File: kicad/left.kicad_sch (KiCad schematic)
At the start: 101 parts, among them Q1 PMF170XP,115, Q2 FS8205A_C2830320, SW1 TS-1088-AR02016, U1 SN74LVC1G17DBVR, U2 E73-2G4M08S1C, U3 SN74LVC1G74DQER, U4 S2B-PH-K-S(LF)(SN), U5 BL8573CS8TR, U6 DW01A_C42380662, U7 LP5024RSMR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

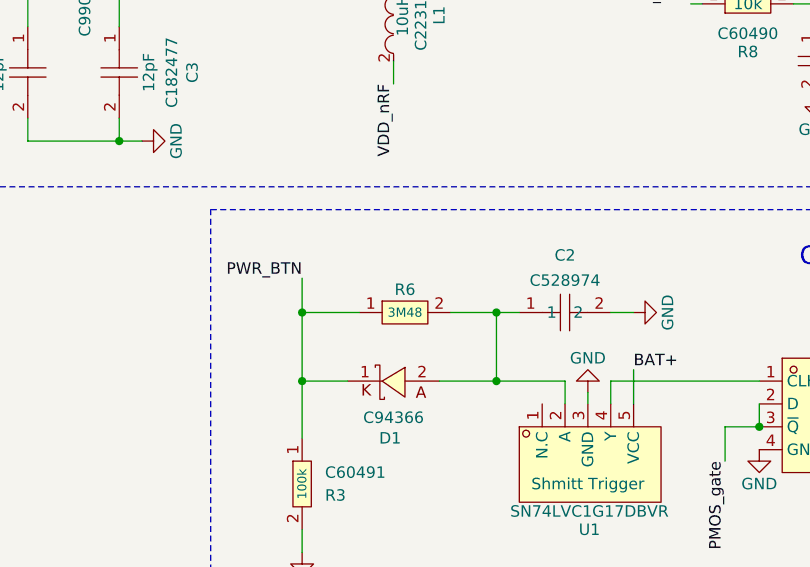
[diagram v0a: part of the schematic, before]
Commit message: changed on/off timing resistor to 2M61 0805
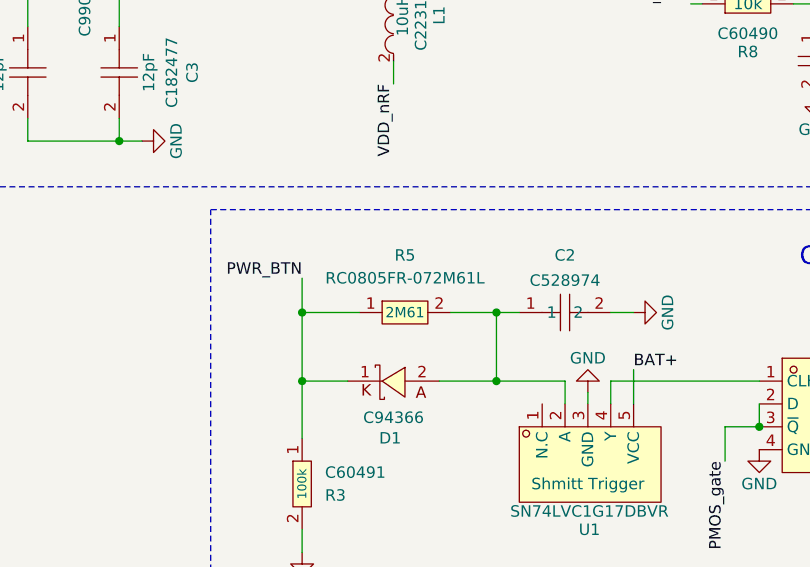
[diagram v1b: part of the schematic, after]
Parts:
- removed R6: 0402WGF1604TCE, easyeda2kicad:R0402, symbol easyeda2kicad:0402WGF1604TCE
- added R5: RC0805FR-072M61L, easyeda2kicad:R0805, symbol easyeda2kicad:RC0805FR-072M61L
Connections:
- net PWR_BTN: now also R5.1
- net at C2.1, D1.2, U1.2 (A): now also R5.2
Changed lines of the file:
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@@
-	)
-	(symbol
-		(lib_id "easyeda2kicad:0402WGF1604TCE")
-		(at 327.66 120.65 0)
-		(unit 1)
-		(body_style 1)
-		(exclude_from_sim no)
-		(in_bom yes)
-		(on_board yes)
-		(in_pos_files yes)
-		(dnp no)
-		(fields_autoplaced yes)
-		(property "Reference" "R6"
-			(at 327.66 118.11 0)
-			(show_name no)
-			(do_not_autoplace no)
-			(effects
-				(font
-					(size 1.27 1.27)
-				)
-			)
-		)
-		(property "Value" "0402WGF1604TCE"
-			(at 327.66 116.84 0)
-			(hide yes)
-			(show_name no)
-			(do_not_autoplace no)
-			(effects
-				(font
-					(size 1.27 1.27)
-				)
-			)
-		)
-		(property "Footprint" "easyeda2kicad:R0402"
-			(at 327.66 128.27 0)
-			(hide yes)
-			(show_name no)
-			(do_not_autoplace no)
-			(effects
-				(font
-					(size 1.27 1.27)
-				)
-			)
-		)
-		(property "Datasheet" "https://lcsc.com/product-detail/Chip-Resistor-Surface-Mount_Uniroyal-Elec-0402WGF1604TCE_C423231.html"
-			(at 327.66 130.81 0)
-			(hide yes)
-			(show_name no)
-			(do_not_autoplace no)
-			(effects
-				(font
-					(size 1.27 1.27)
-				)
-			)
-		)
-		(property "Description" "3M48"
-			(at 327.66 120.65 0)
-			(show_name no)
-			(do_not_autoplace no)
-			(effects
-				(font
-					(size 1.016 1.016)
-				)
-			)
-		)
-		(property "LCSC Part" "C423231"
-			(at 327.66 133.35 0)
-			(hide yes)
-			(show_name no)
-			(do_not_autoplace no)
-			(effects
-				(font
-					(size 1.27 1.27)
-				)
-			)
-		)
-		(pin "2"
-		)
-		(pin "1"
-		)
-		(instances
-			(project "left"
-				(path "/3171f1b4-f2dd-4471-8b63-415e18370dba"
-					(reference "R6")
-					(unit 1)
-				)
-			)
-		)
 	)
 	(symbol
@@
 					(unit 1)
 				)
+			)
+		)
+	)
+	(symbol
+		(lib_id "easyeda2kicad:RC0805FR-072M61L")
+		(at 327.66 120.65 0)
+		(unit 1)
+		(body_style 1)
+		(exclude_from_sim no)
+		(in_bom yes)
+		(on_board yes)
+		(in_pos_files yes)
+		(dnp no)
+		(fields_autoplaced yes)
+		(property "Reference" "R5"
+			(at 327.66 114.3 0)
+			(show_name no)
+			(do_not_autoplace no)
+			(effects
+				(font
+					(size 1.27 1.27)
+				)
+			)
+		)
+		(property "Value" "RC0805FR-072M61L"
+			(at 327.66 116.84 0)
+			(show_name no)
+			(do_not_autoplace no)
+			(effects
+				(font
+					(size 1.27 1.27)
+				)
+			)
+		)
+		(property "Footprint" "easyeda2kicad:R0805"
+			(at 327.66 128.27 0)
+			(hide yes)
+			(show_name no)
+			(do_not_autoplace no)
+			(effects
+				(font
+					(size 1.27 1.27)
+				)
+			)
+		)
+		(property "Datasheet" "https://lcsc.com/product-detail/New-Arrivals_YAGEO-RC0805FR-072M61L_C483050.html"
+			(at 327.66 130.81 0)
+			(hide yes)
+			(show_name no)
+			(do_not_autoplace no)
+			(effects
+				(font
+					(size 1.27 1.27)
+				)
+			)
+		)
+		(property "Description" "2M61"
+			(at 327.66 120.65 0)
+			(show_name no)
+			(do_not_autoplace no)
+			(effects
+				(font
+					(size 1.143 1.143)
+				)
+			)
+		)
+		(property "Manufacturer" "YAGEO(国巨)"
+			(at 327.66 133.35 0)
+			(hide yes)
+			(show_name no)
+			(do_not_autoplace no)
+			(effects
+				(font
+					(size 1.27 1.27)
+				)
+			)
+		)
+		(property "MPN" "RC0805FR-072M61L"
+			(at 327.66 135.89 0)
+			(hide yes)
+			(show_name no)
+			(do_not_autoplace no)
+			(effects
+				(font
+					(size 1.27 1.27)
+				)
+			)
+		)
+		(property "LCSC Part" "C483050"
+			(at 327.66 138.43 0)
+			(hide yes)
+			(show_name no)
+			(do_not_autoplace no)
+			(effects
+				(font
+					(size 1.27 1.27)
+				)
+			)
+		)
+		(pin "1"
+		)
+		(pin "2"
+		)
+		(instances
+			(project "left"
+				(path "/3171f1b4-f2dd-4471-8b63-415e18370dba"
+					(reference "R5")
+					(unit 1)
+				)

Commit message: added gnd vias all over the board. went trough schematic again. changed resistor for rc to bigger one in footprint, and smaller one in Ohm. both left and right sides are ready. just need to go over the kicads check and lastly let someone on discord have a look on the project
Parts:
- removed R15: RT0402BRD0737K4L, :R0402, symbol easyeda2kicad:RT0402BRD0737K4L
- added R6: ERA2AED753X, easyeda2kicad:R0402, symbol easyeda2kicad:ERA2AED753X
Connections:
- net BAT+: now also U6.5 (VDD); no longer U6.6 (VSS)
- net GND: now also U6.6 (VSS), R6.2; no longer U6.5 (VDD)
- net at U7.31 (IREF): now also R6.1
- no-connect marks 0 -> 20
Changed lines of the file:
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@@
 		(color 0 0 0 0)
 	)
+	(no_connect
+		(at 372.11 187.96)
+	)
+	(no_connect
+		(at 340.36 24.13)
+	)
+	(no_connect
+		(at 340.36 26.67)
+	)
+	(no_connect
+		(at 387.35 135.89)
+	)
+	(no_connect
+		(at 349.25 187.96)
+	)
+	(no_connect
+		(at 271.78 184.15)
+	)
+	(no_connect
+		(at 298.45 71.12)
+	)
+	(no_connect
+		(at 260.35 236.22)
+	)
+	(no_connect
+		(at 340.36 36.83)
+	)
+	(no_connect
+		(at 340.36 41.91)
+	)
+	(no_connect
+		(at 134.62 44.45)
+	)
+	(no_connect
+		(at 318.77 71.12)
+	)
+	(no_connect
+		(at 271.78 199.39)
+	)
+	(no_connect
+		(at 134.62 46.99)
+	)
+	(no_connect
+		(at 340.36 31.75)
+	)
+	(no_connect
+		(at 308.61 71.12)
+	)
+	(no_connect
+		(at 340.36 54.61)
+	)
+	(no_connect
+		(at 134.62 49.53)
+	)
+	(no_connect
+		(at 313.69 71.12)
+	)
+	(no_connect
+		(at 340.36 46.99)
+	)
 	(bus_entry
 		(at 118.11 73.66)
@@
 	(wire
 		(pts
-			(xy 260.35 243.84) (xy 260.35 241.3)
-		)
-		(stroke
-			(width 0)
-			(type default)
-		)
-	)
-	(wire
-		(pts
 			(xy 316.23 120.65) (xy 316.23 128.27)
 		)
@@
 	)
 	(label "BAT+"
-		(at 260.35 243.84 180)
+		(at 260.35 238.76 180)
 		(effects
 			(font
@@
 	(symbol
 		(lib_id "PCM_SparkFun-PowerSymbol:GND")
-		(at 260.35 238.76 270)
+		(at 260.35 241.3 270)
 		(unit 1)
 		(body_style 1)
@@
 		(fields_autoplaced yes)
 		(property "Reference" "#PWR022"
-			(at 254 238.76 0)
+			(at 254 241.3 0)
 			(hide yes)
 			(show_name no)
@@
 		)
 		(property "Value" "GND"
-			(at 256.54 238.76 0)
+			(at 256.54 241.3 0)
 			(show_name no)
 			(do_not_autoplace yes)
@@
 		)
 		(property "Footprint" ""
-			(at 260.35 238.76 0)
+			(at 260.35 241.3 0)
 			(hide yes)
 			(show_name no)
@@
 		)
 		(property "Datasheet" ""
-			(at 260.35 238.76 0)
+			(at 260.35 241.3 0)
 			(hide yes)
 			(show_name no)
@@
 		)
 		(property "Description" "Power symbol creates a global label with name \"GND\" , ground"
-			(at 251.46 238.76 0)
+			(at 251.46 241.3 0)
 			(hide yes)
 			(show_name no)
@@
 	)
 	(symbol
+		(lib_id "easyeda2kicad:ERA2AED753X")
+		(at 195.58 31.75 0)
+		(unit 1)
+		(body_style 1)
+		(exclude_from_sim no)
+		(in_bom yes)
+		(on_board yes)
+		(in_pos_files yes)
+		(dnp no)
+		(fields_autoplaced yes)
+		(property "Reference" "R6"
+			(at 195.58 25.4 0)
+			(show_name no)
+			(do_not_autoplace no)
+			(effects
+				(font
+					(size 1.27 1.27)
+				)
+			)
+		)
+		(property "Value" "ERA2AED753X"
+			(at 195.58 27.94 0)
+			(show_name no)
+			(do_not_autoplace no)
+			(effects
+				(font
+					(size 1.27 1.27)
+				)
+			)
+		)
+		(property "Footprint" "easyeda2kicad:R0402"
+			(at 195.58 39.37 0)
+			(hide yes)
+			(show_name no)
+			(do_not_autoplace no)
+			(effects
+				(font
+					(size 1.27 1.27)
+				)
+			)
+		)
+		(property "Datasheet" "https://lcsc.com/product-detail/New-Arrivals_PANASONIC-ERA2AED753X_C491105.html"
+			(at 195.58 41.91 0)
+			(hide yes)
+			(show_name no)
+			(do_not_autoplace no)
+			(effects
+				(font
+					(size 1.27 1.27)
+				)
+			)
+		)
+		(property "Description" "75k"
+			(at 195.58 31.75 0)
+			(show_name no)
+			(do_not_autoplace no)
+			(effects
+				(font
+					(size 1.27 1.27)
+				)
+			)
+		)
+		(property "Manufacturer" "PANASONIC(松下)"
+			(at 195.58 44.45 0)
+			(hide yes)
+			(show_name no)
+			(do_not_autoplace no)
+			(effects
+				(font
+					(size 1.27 1.27)
+				)
+			)
+		)
+		(property "MPN" "ERA2AED753X"
+			(at 195.58 46.99 0)
+			(hide yes)
+			(show_name no)
+			(do_not_autoplace no)
+			(effects
+				(font
+					(size 1.27 1.27)
+				)
+			)
+		)
+		(property "LCSC Part" "C491105"
+			(at 195.58 49.53 0)
+			(hide yes)
+			(show_name no)
+			(do_not_autoplace no)
+			(effects
+				(font
+					(size 1.27 1.27)
+				)
+			)
+		)
+		(pin "1"
+		)
+		(pin "2"
+		)
+		(instances
+			(project "left"
+				(path "/3171f1b4-f2dd-4471-8b63-415e18370dba"
+					(reference "R6")
+					(unit 1)
+				)
+			)
+		)
+	)
+	(symbol
 		(lib_id "PCM_SparkFun-PowerSymbol:GND")
 		(at 353.06 120.65 90)
@@
 					(unit 1)
 				)
-			)
-		)
-	)
-	(symbol
-		(lib_id "easyeda2kicad:RT0402BRD0737K4L")
-		(at 195.58 31.75 0)
-		(unit 1)
-		(body_style 1)
-		(exclude_from_sim no)
-		(in_bom yes)
-		(on_board yes)
-		(in_pos_files yes)
-		(dnp no)
-		(fields_autoplaced yes)
-		(property "Reference" "R15"
-			(at 195.58 26.162 0)
-			(show_name no)
-			(do_not_autoplace no)
-			(effects
-				(font
-					(size 1.27 1.27)
-				)
-			)
-		)
-		(property "Value" "RT0402BRD0737K4L"
-			(at 195.58 27.94 0)
-			(hide yes)
-			(show_name no)
-			(do_not_autoplace no)
-			(effects
-				(font
-					(size 1.27 1.27)
-				)
-			)
-		)
-		(property "Footprint" ":R0402"
-			(at 195.58 39.37 0)
-			(hide yes)
-			(show_name no)
-			(do_not_autoplace no)
-			(effects
-				(font
-					(size 1.27 1.27)
-				)
-			)
-		)
-		(property "Datasheet" ""
-			(at 195.58 31.75 0)
-			(hide yes)
-			(show_name no)
-			(do_not_autoplace no)
-			(effects
-				(font
-					(size 1.27 1.27)
-				)
-			)
-		)
-		(property "Description" "37k4"
-			(at 195.58 31.75 0)
-			(show_name no)
-			(do_not_autoplace no)
-			(effects
-				(font
-					(size 1.27 1.27)
-				)
-			)
-		)
-		(property "LCSC Part" "C852746"
-			(at 195.58 28.702 0)
-			(show_name no)
-			(do_not_autoplace no)
-			(effects
-				(font
-					(size 1.27 1.27)
-				)
-			)
-		)
-		(pin "1"
-		)
-		(pin "2"
-		)
-		(instances
-			(project "left"
-				(path "/3171f1b4-f2dd-4471-8b63-415e18370dba"
-					(reference "R15")
-					(unit 1)
-				)

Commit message: both sides done. changed few components for their basic or more affordable alternaatives.
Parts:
- added U9: USBLC6-2SC6, Package_TO_SOT_SMD:SOT-23-6, symbol Power_Protection:USBLC6-2SC6
- C1, C3: value 0402CG120F500NT -> 0402CG120J500NT; LCSC Part C182477 -> C1547
- C2: value GRM155Z71A105KE01D -> CL05A105KA5NQNC; LCSC Part C528974 -> C52923
- C4, C6, C9: value GRM033C71C104KE14D -> CL05B104KB54PNC; footprint easyeda2kicad:C0201 -> easyeda2kicad:C0402; LCSC Part C85923 -> C307331
- C7, C8: value GRM155C71C105KE11D -> CL05A105KA5NQNC; LCSC Part C576449 -> C52923
- R1, R17: value RC0402FR-071ML -> 0402WGF1004TCE; LCSC Part C138033 -> C26083
- R10, R14, R16, R9: value RC0402FR-075K1L -> 0402WGF5101TCE; LCSC Part C105872 -> C25905
- R11: value RC0201FR-07680RL -> RC0402FR-07680RL; footprint easyeda2kicad:R0201 -> easyeda2kicad:R0402; LCSC Part C274876 -> C137948
- R12, R13, R4, R7, R8: value RC0402FR-0710KL -> 0402WGF1002TCE; LCSC Part C60490 -> C25744
- R5: value RC0805FR-072M61L -> RTT022614FTH; footprint easyeda2kicad:R0805 -> easyeda2kicad:R0402; LCSC Part C483050 -> C166493; MPN RC0805FR-072M61L -> RTT022614FTH; Manufacturer YAGEO(国巨) -> RALEC
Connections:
- net SCL_BAT is gone; now on net SCL: U2.8 (AI5), U8.7 (SCL)
- net SDA_BAT is gone; now on net SDA: U2.7 (AI0), U8.8 (SDA)
- net D+: now also U9.1 (I/O1), U9.6 (I/O1)
- net D-: now also U9.3 (I/O2), U9.4 (I/O2)
- net GND: now also U9.2 (GND)
- net SCL: no longer U2.17 (P1.09)
- net SDA: no longer U2.16 (P0.08)
- net SWBCLK: now also U2.39 (SWC); no longer U2.2 (P1.10)
- net SWDIO: now also U2.37 (SWD); no longer U2.1 (P1.11)
- net VBUS_RAW: now reaches F1.1, USBC1.A4B9 (VBUS), USBC1.B4A9 (VBUS)
- net VBUS_RAW: now also U9.5 (VBUS)
- no-connect marks 20 -> 18
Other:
- moved on the sheet: C6

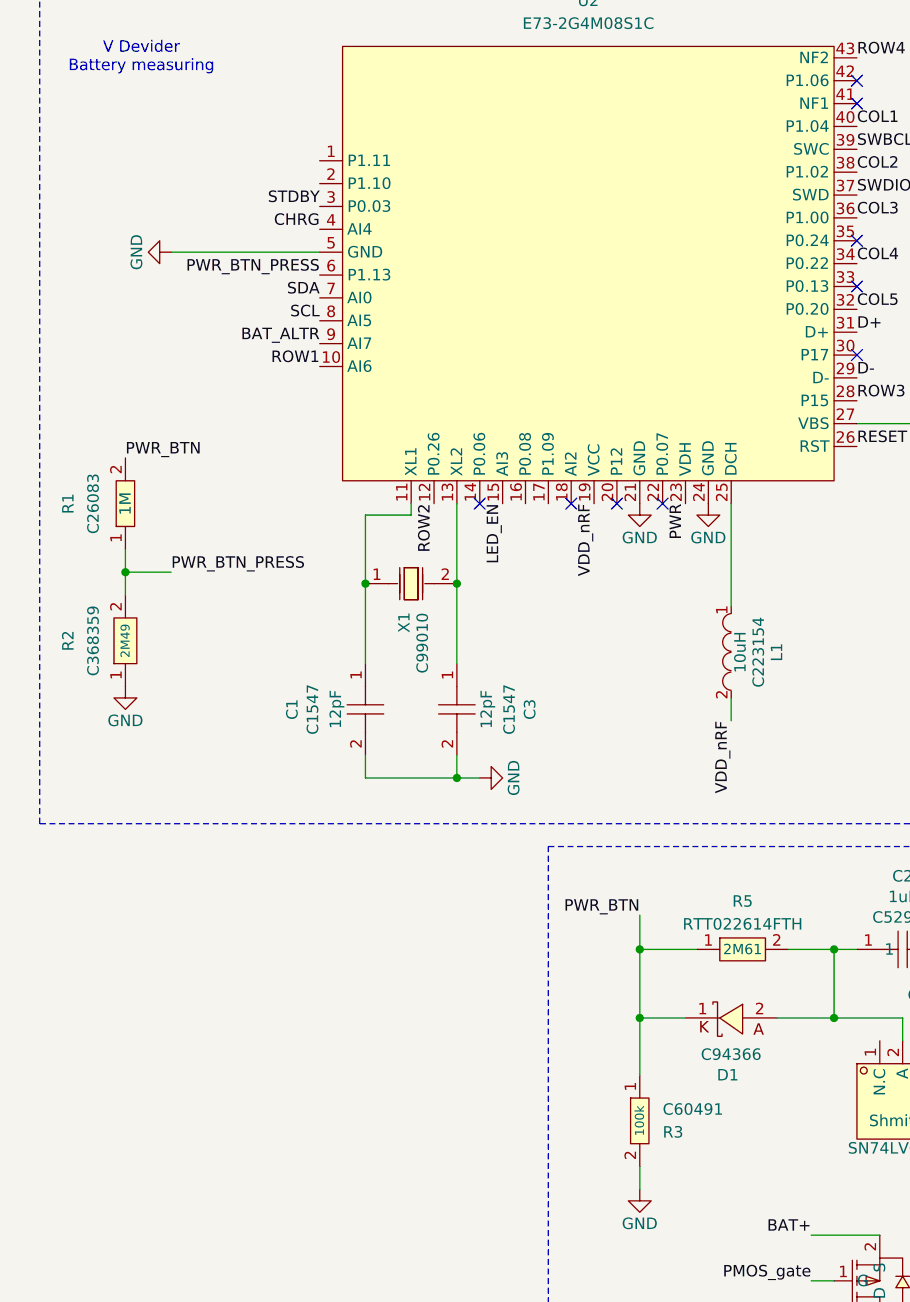
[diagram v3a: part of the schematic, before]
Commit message: first panelization... changing parts because of availability
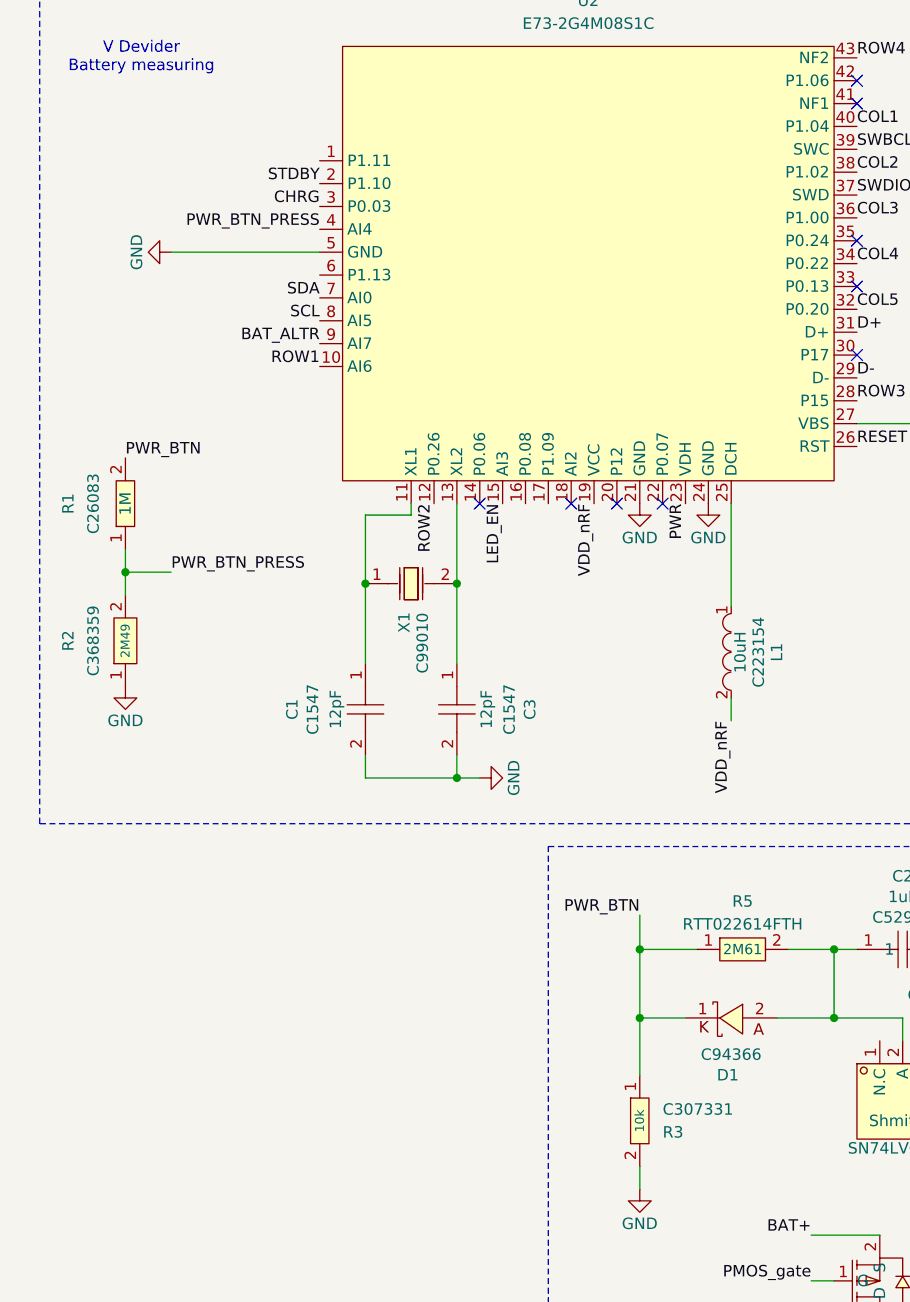
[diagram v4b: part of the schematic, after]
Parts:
- R3: value RC0402FR-07100KL -> 0402WGF1002TCE; LCSC Part C60491 -> C307331
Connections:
- net CHRG: now also U2.3 (P0.03); no longer U2.4 (AI4)
- net PWR_BTN_PRESS: now also U2.4 (AI4); no longer U2.6 (P1.13)
- net STDBY: now also U2.2 (P1.10); no longer U2.3 (P0.03)
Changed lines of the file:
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@@
 		)
 	)
-	(label "STDBY"
+	(label "CHRG"
 		(at 280.67 38.1 180)
 		(effects
@@
 		)
 	)
-	(label "PWR_BTN_PRESS"
-		(at 280.67 45.72 180)
-		(effects
-			(font
-				(size 1.27 1.27)
-			)
-			(justify right bottom)
-		)
-	)
 	(label "COL5"
 		(at 340.36 49.53 0)
@@
 		)
 	)
+	(label "STDBY"
+		(at 280.67 35.56 180)
+		(effects
+			(font
+				(size 1.27 1.27)
+			)
+			(justify right bottom)
+		)
+	)
+	(label "PWR_BTN_PRESS"
+		(at 280.67 40.64 180)
+		(effects
+			(font
+				(size 1.27 1.27)
+			)
+			(justify right bottom)
+		)
+	)
 	(label "LED19"
 		(at 118.11 73.66 180)
@@
 		)
 	)
-	(label "CHRG"
-		(at 280.67 40.64 180)
-		(effects
-			(font
-				(size 1.27 1.27)
-			)
-			(justify right bottom)
-		)
-	)
 	(label "LED5"
 		(at 134.62 59.69 180)
@@
 			)
 		)
-		(property "Value" "RC0402FR-07100KL"
+		(property "Value" "0402WGF1002TCE"
 			(at 312.42 139.7 0)
 			(hide yes)
@@
 			)
 		)
-		(property "Datasheet" "https://lcsc.com/product-detail/Chip-Resistor-Surface-Mount_100KR-1003-1_C60491.html"
+		(property "Datasheet" "https://lcsc.com/datasheet/C25744.pdf"
 			(at 326.39 139.7 0)
 			(hide yes)
@@
 			)
 		)
-		(property "Description" "100k"
+		(property "Description" "10k"
 			(at 316.23 139.7 0)
 			(show_name no)
@@
 			)
 		)
-		(property "LCSC Part" "C60491"
+		(property "LCSC Part" "C307331"
 			(at 318.77 138.4301 90)
 			(show_name no)
